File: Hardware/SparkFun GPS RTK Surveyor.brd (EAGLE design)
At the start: 69.1 x 111.1 mm, 167 parts, among them J16 microSD, J3 USB-C, J4 Qwiic Right Angle, J6 Start Base, J7 Power Switch, Q2 MBT3904DW1T1, U1 MCP73831, U2 3.3V, U3 U-BLOX_ZED-F9P, U5 ESP-WROOM-32NARROW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

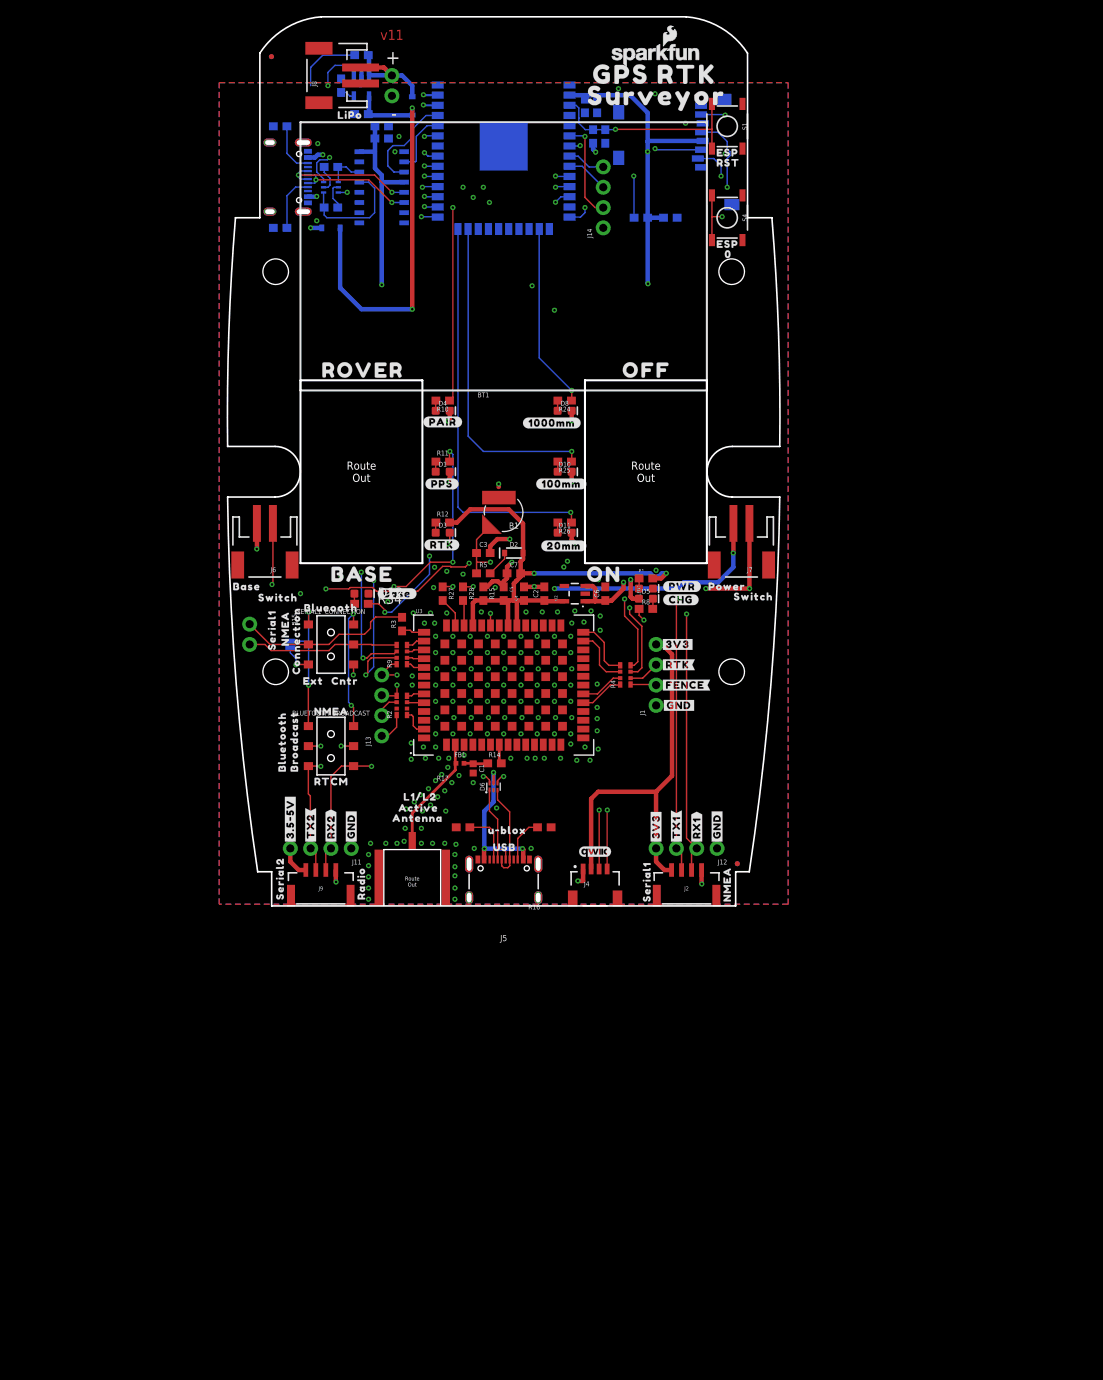
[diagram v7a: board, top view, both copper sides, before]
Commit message: Adjust LEDs to match overlay design.
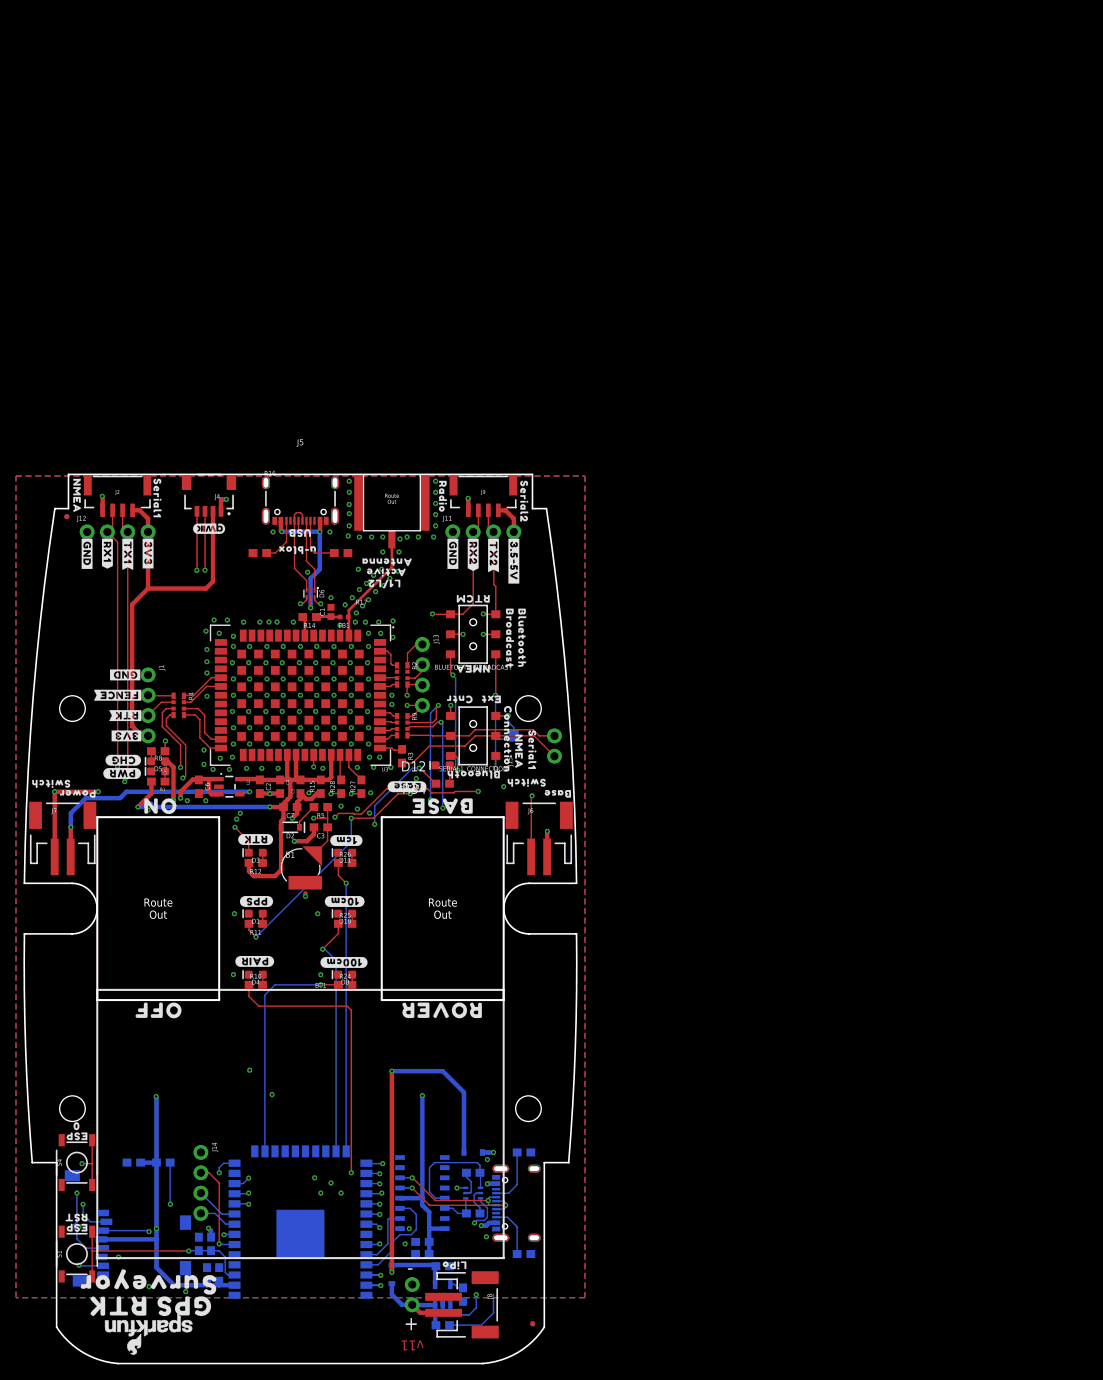
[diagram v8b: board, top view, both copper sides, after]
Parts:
- removed U$66: (no value), output:#20MM#0
- removed U$67: (no value), output:#100MM#1
- removed U$68: (no value), output:#1000MM#2
- added U$69, U$75, U$76, U$77, U$78: (no value), SparkFun GPS RTK Surveyor:LIGHT_PIPE_3MM
- added U$79: (no value), output:#1CM#0
- added U$80: (no value), output:#10CM#1
- added U$81: (no value), output:#100CM#2
- R1, R10, R11, R12, R24, R25, R26, R34, R8: value 1k -> 330
- moved LOGO3 171.0 mm to (-19.1, -52.1), turned to 180 degrees
- moved S1 162.7 mm to (-27.9, -43.2), turned to 90 degrees
- moved JP61 161.7 mm to (29.0, -51.9), turned to 180 degrees
- moved JP81 161.7 mm to (29.0, -51.9), turned to 180 degrees
- moved U$70 160.1 mm to (-9.40, -49.7), turned to 180 degrees
- moved C8 159.1 mm to (17.8, -52.1), turned to 180 degrees
- moved J16 157.9 mm to (-14.0, -47.0), turned to 270 degrees
- moved U$74 155.0 mm to (-25.9, -39.9), turned to 180 degrees
- moved J8 154.7 mm to (21.6, -49.5), turned to 270 degrees
- moved U$71 154.2 mm to (-7.87, -47.0), turned to 180 degrees
- moved C13 154.0 mm to (-11.7, -45.7), turned to 90 degrees
- moved J10 153.7 mm to (14.0, -49.5), turned to 90 degrees
- moved C11 153.0 mm to (-10.2, -45.7), turned to 90 degrees
- moved U$60 152.8 mm to (-25.9, -38.6), turned to 180 degrees
- moved R7 151.9 mm to (20.3, -48.3), turned to 90 degrees
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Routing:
- net ESP32_2/POSACC1: track 50.5 -> 36.5 mm
- net RTK_STAT: track 45.8 -> 32.7 mm
- net ESP32_12/BLUETOOTH_STATUS: track 43.6 -> 54.6 mm
- net ESP32_15/POSACC2: track 40.9 -> 30.1 mm
- net GND: track 38.4 -> 31.6 mm, vias 158 -> 157
- net PPS_STAT: track 47.1 -> 53.6 mm
- net ESP32_13/POSACC3: track 23.1 -> 29.3 mm
- net VIN: track 211.0 -> 213.3 mm
- net CHG_LED: track 120.0 -> 121.8 mm
- net NMEA-RX: track 15.8 -> 17.5 mm
- net 3.3V: track 264.3 -> 262.9 mm
- net N$30: track 1.28 -> 2.30 mm
- net ZED-RXI2: track 79.8 -> 79.0 mm
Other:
- outline, holes or cut-outs redrawn
